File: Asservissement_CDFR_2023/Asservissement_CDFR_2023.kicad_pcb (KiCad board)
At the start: 2 copper layers, 87 x 115 mm, 165 parts, among them IC1 A3930KJPTR-T, IC2 A3930KJPTR-T, J1 Connecteur batterie, J10 Free Connecteur, J11 Conn_01x02, J12 Conn_01x02, J13 Connecteur Odométrie, J2 Conn_01x03, J3 Conn_01x05, J4 Connecteur Programmation, J5 Conn_01x03, J6 Connecteur Odométrie, J7 Conn_01x03, J8 Conn_01x03, J9 Conn_01x05, Q1 QM6006D, Q10 QM6006D, Q11 QM6006D, Q12 QM6006D, Q13 Q_NMOS_GDS, Q2 QM6006D, Q3 QM6006D, Q4 QM6006D, Q5 QM6006D, Q6 QM6006D, Q7 QM6006D, Q8 QM6006D, Q9 QM6006D, U1 LM317_SOT-223, U3 STM32F401RCTx, U4 LMR16020PDDA, Y1 Crystal_GND24

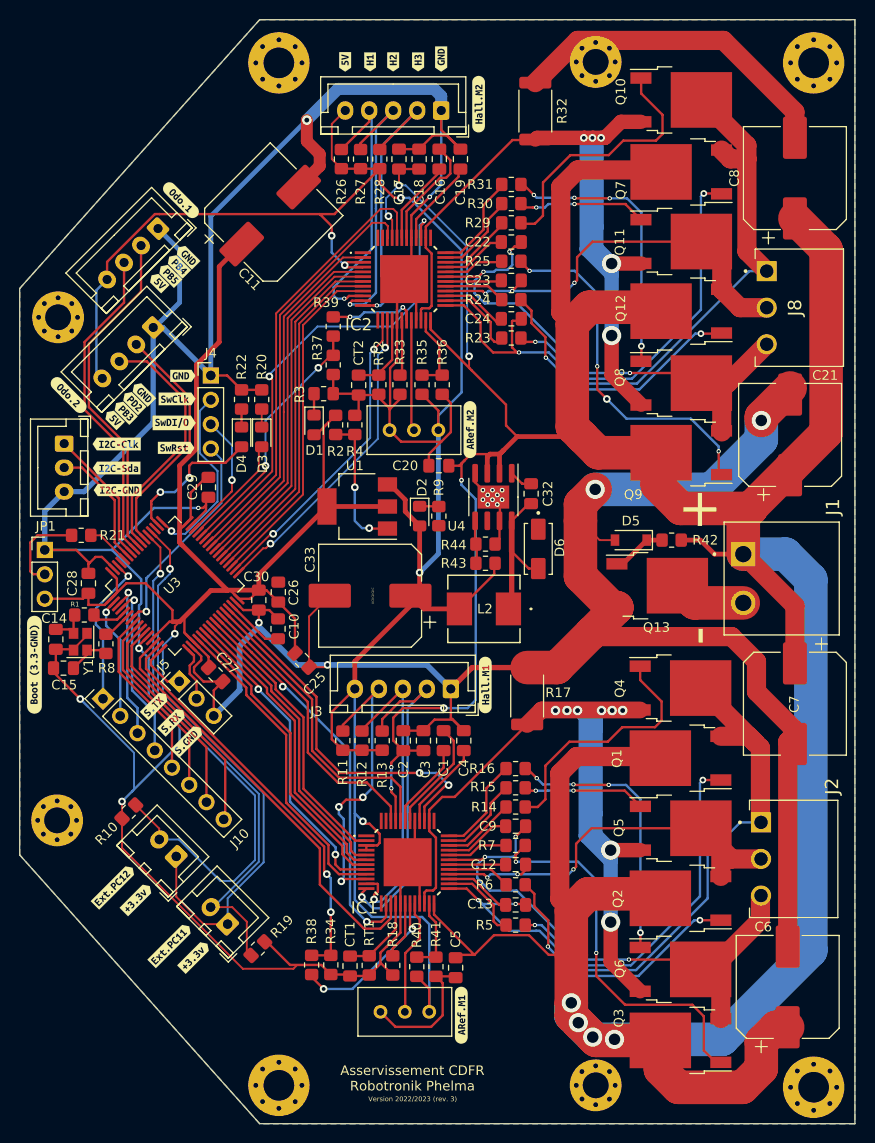
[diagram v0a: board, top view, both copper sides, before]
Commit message: V4 add button, test point, remove quartz, pot and fix current
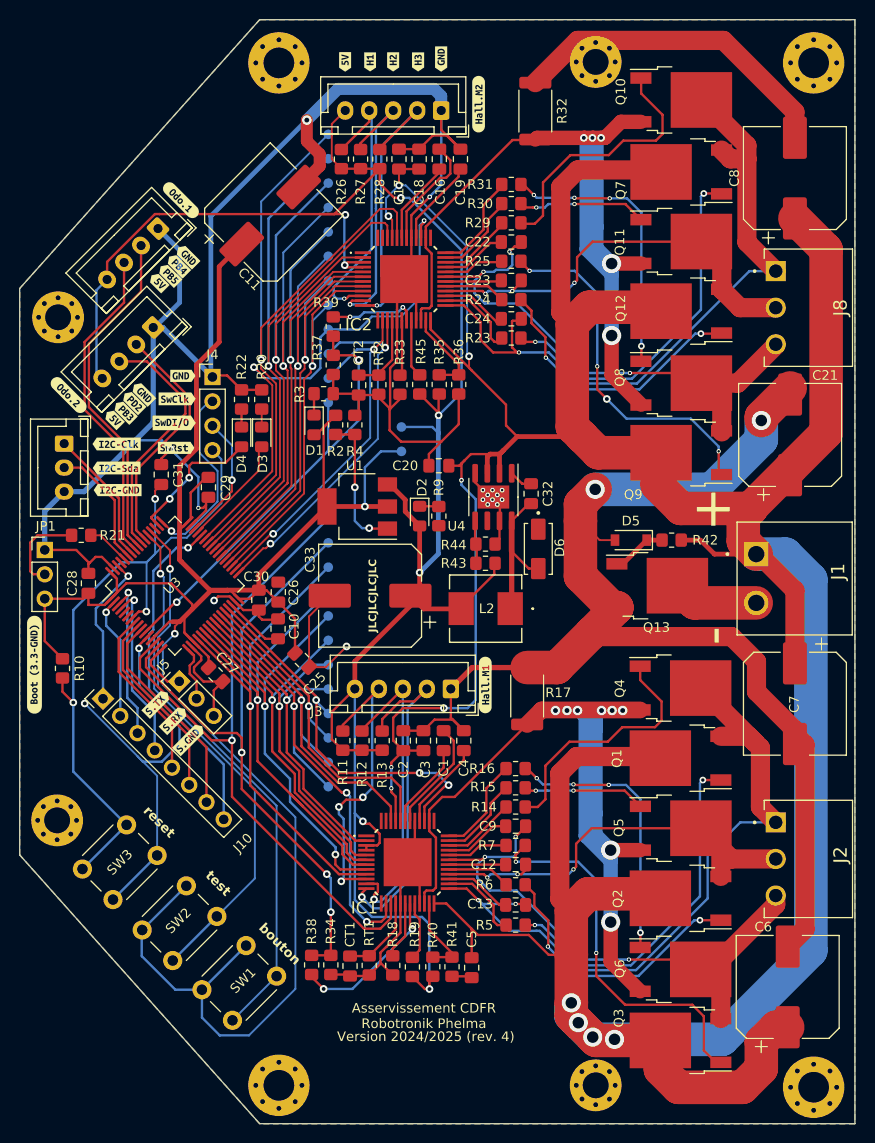
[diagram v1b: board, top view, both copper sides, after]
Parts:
- removed C14, C15: 10pF, Capacitor_SMD:C_0805_2012Metric_Pad1.18x1.45mm_HandSolder
- removed J11, J12: Conn_01x02, Connector_JST:JST_XH_B2B-XH-A_1x02_P2.50mm_Vertical
- removed R1, R8: 10k, Resistor_SMD:R_0805_2012Metric_Pad1.20x1.40mm_HandSolder
- removed RV1, RV2: 10k, Potentiometer_THT:Potentiometer_Bourns_3386C_Horizontal
- removed Y1: Crystal_GND24, Crystal:Crystal_SMD_2520-4Pin_2.5x2.0mm
- removed kibuzzard-637D40DA: G***, kibuzzard-637D40DA
- removed kibuzzard-637D40E8: G***, kibuzzard-637D40E8
- removed kibuzzard-637D40F4 (x2): G***, kibuzzard-637D40F4
- removed kibuzzard-637D4198: G***, kibuzzard-637D4198
- removed kibuzzard-637D41A9: G***, kibuzzard-637D41A9
- added C31: 0.1nF, Capacitor_SMD:C_0805_2012Metric_Pad1.18x1.45mm_HandSolder, F.Cu at (49.3, 76.9)
- added R45: 100k, Resistor_SMD:R_0805_2012Metric_Pad1.20x1.40mm_HandSolder, F.Cu at (76.3, 67.5)
- added SW1: SW_Push, Button_Switch_THT:SW_PUSH_6mm_H5mm, F.Cu at (53.6, 130.6)
- added SW2: SW_Push, Button_Switch_THT:SW_PUSH_6mm_H5mm, F.Cu at (47.4, 124.4)
- added SW3: SW_Push, Button_Switch_THT:SW_PUSH_6mm_H5mm, F.Cu at (41.1, 118.0)
- added TP1: TestPoint, TestPoint:TestPoint_Pad_D1.0mm, B.Cu at (66.7, 69.4)
- added TP10: TestPoint, TestPoint:TestPoint_Pad_D1.0mm, B.Cu at (66.7, 46.6)
- added TP11: TestPoint, TestPoint:TestPoint_Pad_D1.0mm, B.Cu at (66.7, 49.1)
- added TP12: TestPoint, TestPoint:TestPoint_Pad_D1.0mm, B.Cu at (66.7, 51.7)
- added TP13: TestPoint, TestPoint:TestPoint_Pad_D1.0mm, B.Cu at (74.4, 72.0)
- added TP14: TestPoint, TestPoint:TestPoint_Pad_D1.0mm, B.Cu at (74.4, 74.5)
- added TP2: TestPoint, TestPoint:TestPoint_Pad_D1.0mm, B.Cu at (66.7, 64.4)
- added TP25: TestPoint, TestPoint:TestPoint_Pad_D1.0mm, B.Cu at (66.7, 101.8)
- added TP26: TestPoint, TestPoint:TestPoint_Pad_D1.0mm, B.Cu at (66.7, 104.4)
- added TP27: TestPoint, TestPoint:TestPoint_Pad_D1.0mm, B.Cu at (66.7, 106.9)
- added TP28: TestPoint, TestPoint:TestPoint_Pad_D1.0mm, B.Cu at (66.7, 99.3)
- added TP29: TestPoint, TestPoint:TestPoint_Pad_D1.0mm, B.Cu at (66.7, 96.7)
- added TP3: TestPoint, TestPoint:TestPoint_Pad_D1.0mm, B.Cu at (66.7, 59.3)
- added TP30: TestPoint, TestPoint:TestPoint_Pad_D1.0mm, B.Cu at (66.7, 94.2)
- added TP31: TestPoint, TestPoint:TestPoint_Pad_D1.0mm, B.Cu at (66.7, 89.1)
- added TP32: TestPoint, TestPoint:TestPoint_Pad_D1.0mm, B.Cu at (66.7, 91.7)
- added TP33: TestPoint, TestPoint:TestPoint_Pad_D1.0mm, B.Cu at (66.7, 86.6)
- added TP34: TestPoint, TestPoint:TestPoint_Pad_D1.0mm, B.Cu at (66.7, 109.4)
- added TP35: TestPoint, TestPoint:TestPoint_Pad_D1.0mm, B.Cu at (66.7, 81.5)
- added TP36: TestPoint, TestPoint:TestPoint_Pad_D1.0mm, B.Cu at (66.7, 84.0)
- added TP4: TestPoint, TestPoint:TestPoint_Pad_D1.0mm, B.Cu at (66.7, 66.9)
- added TP5: TestPoint, TestPoint:TestPoint_Pad_D1.0mm, B.Cu at (66.7, 54.2)
- added TP6: TestPoint, TestPoint:TestPoint_Pad_D1.0mm, B.Cu at (66.7, 56.7)
- added TP7: TestPoint, TestPoint:TestPoint_Pad_D1.0mm, B.Cu at (66.7, 61.8)
- added TP8: TestPoint, TestPoint:TestPoint_Pad_D1.0mm, B.Cu at (66.7, 41.5)
- added TP9: TestPoint, TestPoint:TestPoint_Pad_D1.0mm, B.Cu at (66.7, 44.0)
- R19: value 10k -> 100k
- moved R10 16.5 mm to (39.1, 97.1), turned to -90 degrees
- moved R19 16.2 mm to (75.5, 128.2), turned to -90 degrees
- moved G*** 4.26 mm to (77.1, 85.5)
- moved R35 1.79 mm to (78.3, 67.5)
- moved R36 1.72 mm to (80.3, 67.5)
- moved R40 1.67 mm to (77.6, 128.2)
- moved R41 1.67 mm to (79.6, 128.2)
- moved C5 1.67 mm to (81.7, 128.3)
- moved J2 1.53 mm to (113.4, 113.2)
- moved J1 1.35 mm to (111.3, 85.2)
- moved J8 0.94 mm to (113.4, 55.7)
- moved J4 0.23 mm to (54.7, 66.8)
- moved kibuzzard-637D41F7 0.23 mm to (50.7, 102.5)
- moved kibuzzard-637D4204 0.23 mm to (52.3, 104.5)
- moved kibuzzard-637D4217 0.23 mm to (48.9, 100.8)
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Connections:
- net Net-(R34-Pad1) renamed Info_Courant_1_uc
- IC1 pad 20: Net-(IC1-Pad20) -> Net-(IC1-REF_)
- J4 pad 4: Net-(J4-Pad4) -> NRST
- R10 pad 1: GND -> +3.3V
- R10 pad 2: Net-(J11-Pad2) -> NRST
- R19 pad 1: GND -> Net-(IC1-REF_)
- R19 pad 2: Net-(J12-Pad2) -> +5V
- R37 pad 1: Net-(R37-Pad1) -> Info_Courant_2_uc
- R39 pad 1: Net-(R37-Pad1) -> Info_Courant_2_uc
- U3 pad 11: Free8 -> Info_Courant_2_uc
- U3 pad 44: Net-(R37-Pad1) -> Free8
- U3 pad 5: Net-(R1-Pad2) -> unconnected-(U3-PH0-Pad5)
- U3 pad 52: Net-(J12-Pad2) -> Net-(U3-PC11)
- U3 pad 53: Net-(J11-Pad2) -> Net-(U3-PC12)
- U3 pad 6: Net-(R8-Pad2) -> unconnected-(U3-PH1-Pad6)
- U3 pad 7: Net-(J4-Pad4) -> NRST
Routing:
- net GND: track 591.2 -> 496.6 mm
- net NRST: track 0.00 -> 76.2 mm, vias 0 -> 3
- net Net-(U3-PC11): track 0.00 -> 59.2 mm, vias 0 -> 1
- net Net-(J11-Pad2): track 56.3 -> 0.00 mm, vias 1 -> 0
- net Net-(J12-Pad2): track 54.9 -> 0.00 mm, vias 1 -> 0
- net +3.3V: track 182.7 -> 236.9 mm, vias 1 -> 2
- net Net-(U3-PC12): track 0.00 -> 53.3 mm, vias 0 -> 1
- net Info_Courant_2_uc: track 0.00 -> 47.7 mm, vias 0 -> 2
- net MODE_1: track 44.9 -> 73.4 mm, vias 0 -> 1
- net info_direction_2: track 46.3 -> 74.0 mm, vias 0 -> 1
- net Info_Courant_1_uc: track 42.7 -> 69.8 mm, vias 2 -> 3
- net Net-(R37-Pad1): track 26.6 -> 0.00 mm, vias 2 -> 0
- net disable_2: track 43.6 -> 68.7 mm, vias 0 -> 1
- net Net-(J4-Pad4): track 22.6 -> 0.00 mm, vias 1 -> 0
- net reset_2: track 38.0 -> 59.4 mm, vias 0 -> 1
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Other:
- board text added: "3.3V"
- board text added: "5V"
- board text added: "GND"
- board text added: "Version 2024/2025 (rev. 4)"
- board text added: "action_err_1"
- board text added: "action_err_2"
- board text added: "bouton"
- board text added: "courant_1"
- board text added: "courant_2"
- board text added: "direction_1"
- board text added: "direction_2"
- board text added: "disable_1"
- board text added: "disable_2"
- board text added: "encodeur_1"
- board text added: "encodeur_2"
- board text added: "erreur_1_1"
- board text added: "erreur_1_2"
- board text added: "erreur_2_1"
- board text added: "erreur_2_2"
- board text added: "frein_1"
- board text added: "frein_2"
- board text added: "info_direction_2"
- board text added: "mode_1"
- board text added: "mode_2"
- board text added: "reset"
- board text added: "reset_1"
- board text added: "reset_2"
- board text added: "test"
- board text added: "vitesse_1"
- board text added: "vitesse_2"
- board text removed: "Version 2022/2023 (rev. 3)"
